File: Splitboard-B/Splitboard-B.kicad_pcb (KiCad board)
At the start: 2 copper layers, 185 x 150 mm, 83 parts, among them J1 USB_C_Receptacle, K1 KEYSW, K10 KEYSW, K11 KEYSW, K12 KEYSW, K13 KEYSW, K14 KEYSW, K15 KEYSW, K16 KEYSW, K17 KEYSW, K18 KEYSW, K19 KEYSW, K2 KEYSW, K20 KEYSW, K21 KEYSW, K22 KEYSW, K23 KEYSW, K24 KEYSW, K25 KEYSW, K26 KEYSW, K27 KEYSW, K28 KEYSW, K29 KEYSW, K3 KEYSW, K30 KEYSW, K31 KEYSW, K32 KEYSW, K33 KEYSW, K34 KEYSW, K35 KEYSW, K36 KEYSW, K37 KEYSW, K38 KEYSW, K4 KEYSW, K5 KEYSW, K6 KEYSW, K7 KEYSW, K8 KEYSW, K9 KEYSW, SW1 RotaryEncoder, U3 CR2013-MI2120

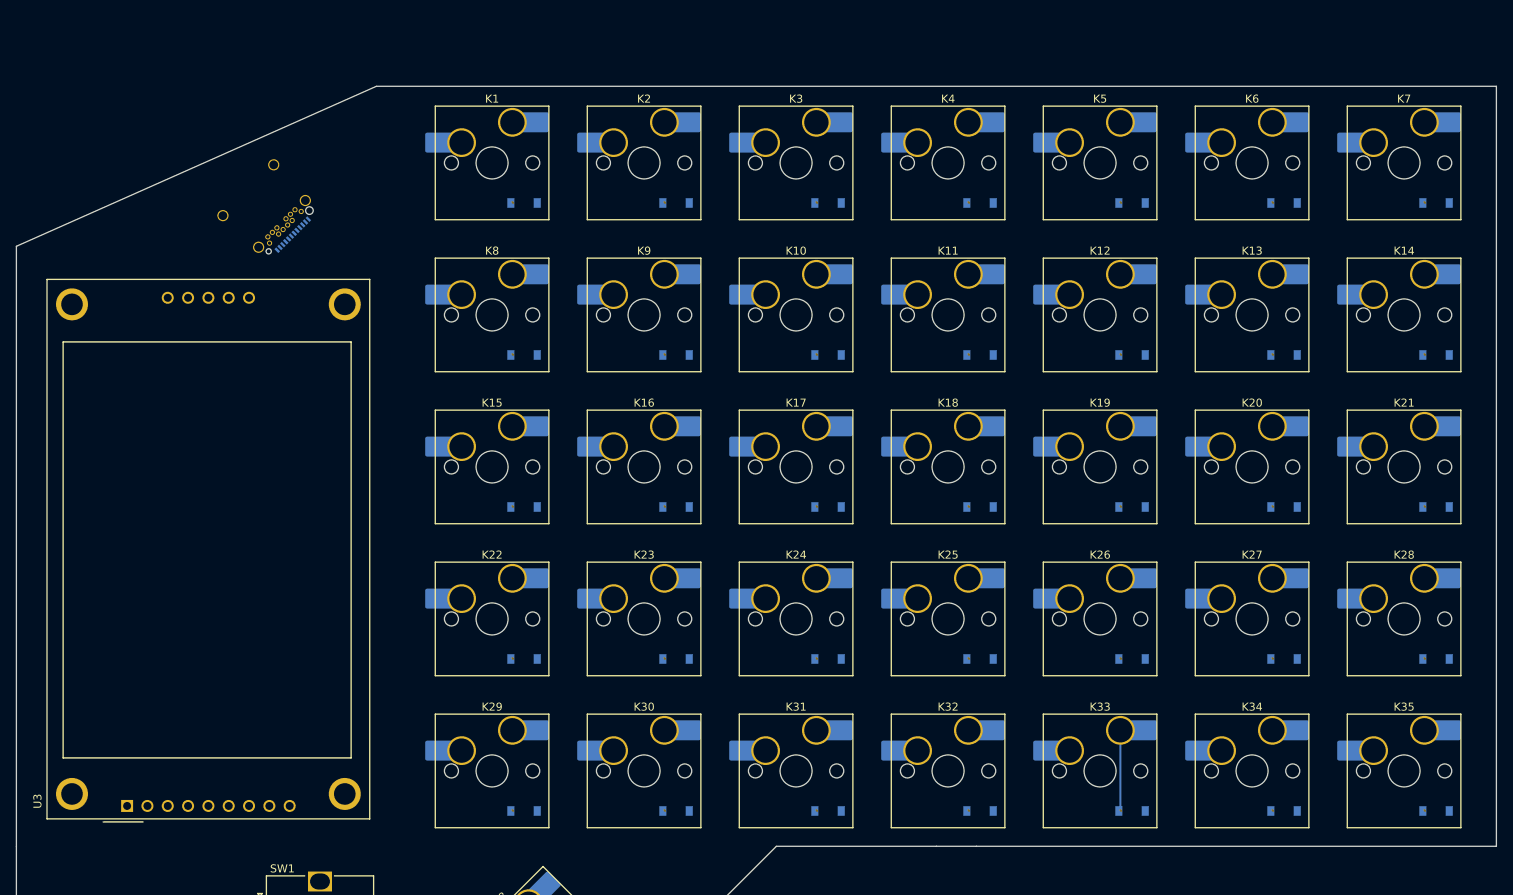
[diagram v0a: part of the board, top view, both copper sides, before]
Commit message: created 3d model for the keyboard as well as kbt1 acrylic models
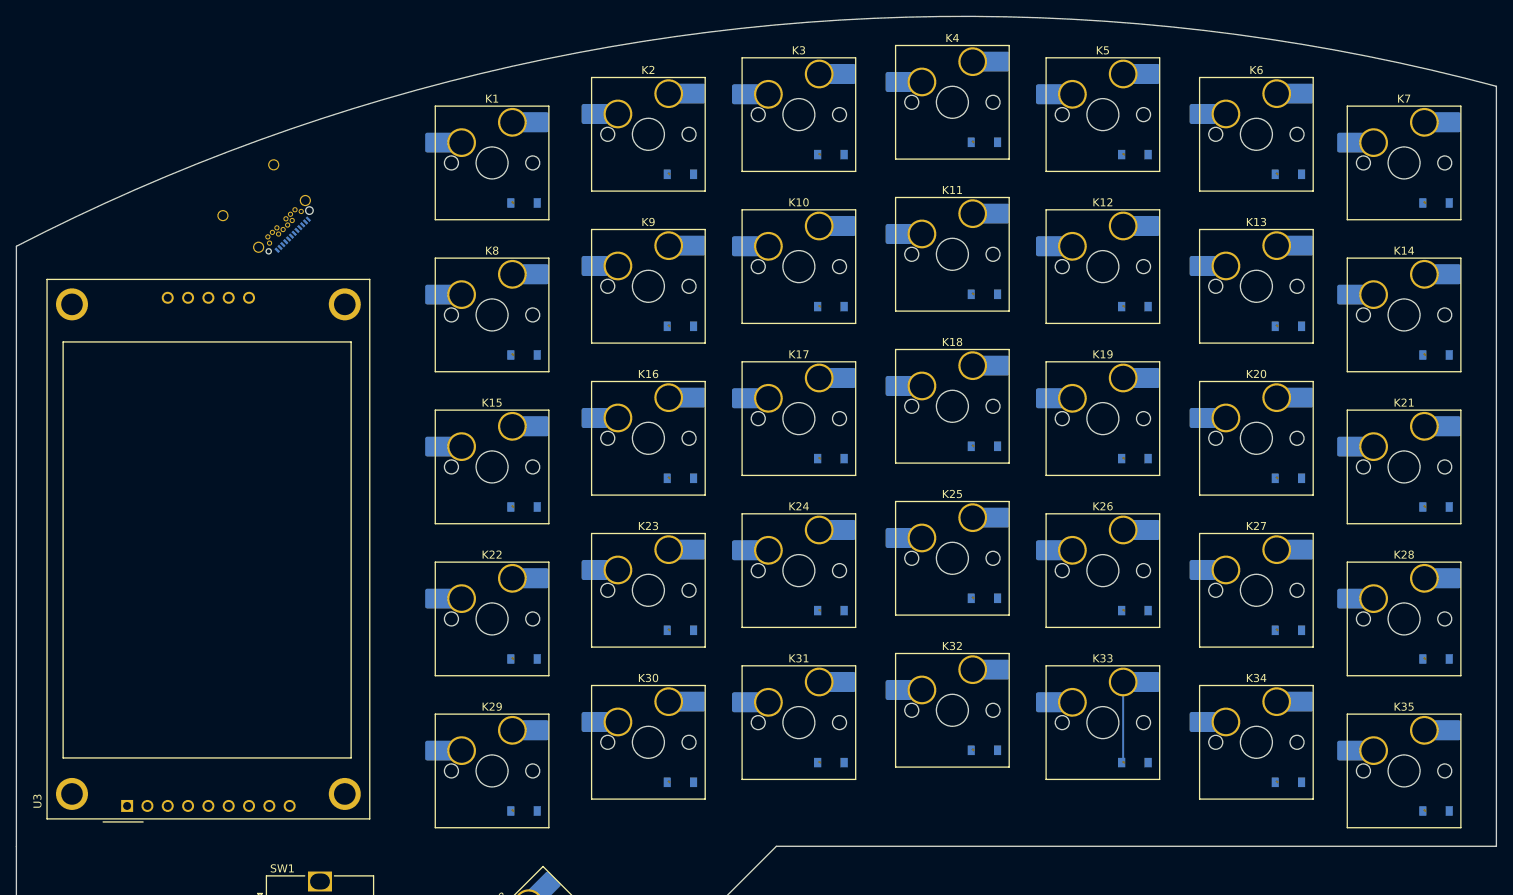
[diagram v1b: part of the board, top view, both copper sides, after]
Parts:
- moved D11 7.60 mm to (166.0, 61.0)
- moved D18 7.60 mm to (166.0, 80.0)
- moved D25 7.60 mm to (166.0, 99.0)
- moved D32 7.60 mm to (166.0, 118.0)
- moved D4 7.60 mm to (166.0, 42.0)
- moved K11 7.60 mm to (162.0, 56.0)
- moved K18 7.60 mm to (162.0, 75.0)
- moved K25 7.60 mm to (162.0, 94.0)
- moved K32 7.60 mm to (162.0, 113.0)
- moved K4 7.60 mm to (162.0, 37.0)
- moved D10 6.05 mm to (146.8, 62.5)
- moved D12 6.05 mm to (184.8, 62.5)
- moved D3 6.05 mm to (146.8, 43.5)
- moved D5 6.05 mm to (184.8, 43.5)
- moved K10 6.05 mm to (142.8, 57.5)
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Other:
- board size 185 x 150 mm -> 185 x 158.7 mm

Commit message: Keyboard changes (added split to other half, component footprints)
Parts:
- added U1: MCP23018-E/SP, 6:MCP23018-E&slash_SP, F.Cu at (65.0, 77.0)
- J1: footprint Connector_USB:USB_C_Receptacle_Amphenol_12401548E4-2A_CircularHoles -> Connector_USB:USB_C_Receptacle_GCT_USB4085
- moved H2 232.5 mm to (211.0, 34.0)
- moved H4 175.2 mm to (189.0, 126.0)
- moved H1 164.4 mm to (59.0, 53.0)
- moved H3 67.9 mm to (71.0, 160.0)
- moved J1 8.62 mm to (84.6, 50.8), turned to 20 degrees

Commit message: Added debugging header to splitboard B
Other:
- board text added: "ALL VIA INTERAL DIAMETERS NEED TO BE >= 5mm (for fly wiring) Also untented"
- board text added: "The switches unfortunately need to be re-spaced. They are 19mm apart from center to center, we need the horizontal distance to be 19mm, center to center distance will be greater than 19mm because of trig & stuff"
- board text added: "we need to consider creating more board for these holes consider the screw head that will rest on top of the hole"
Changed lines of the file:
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@@
   (gr_line (start 45 145) (end 45 130) (layer "Edge.Cuts") (width 0.1))
   (gr_arc (start 45 55) (mid 135.635806 27.756199) (end 230 35) (layer "Edge.Cuts") (width 0.1))
+  (gr_text "ALL VIA INTERAL DIAMETERS\nNEED TO BE >= 5mm (for fly wiring)\nAlso untented" (at 266.7 96.52) (layer "F.SilkS")
+    (effects (font (size 2 2) (thickness 0.3)))
+  )
+  (gr_text "The switches unfortunately need to be re-spaced.\nThey are 19mm apart from center to center, we need\nthe horizontal distance to be 19mm, center to center\ndistance will be greater than 19mm because of trig & stuff" (at 281.94 45.72) (layer "F.SilkS")
+    (effects (font (size 2 2) (thickness 0.3)))
+  )
+  (gr_text "we need to consider creating more board for these holes\nconsider the screw head that will rest on top of the hole" (at 210.82 139.7) (layer "F.SilkS")
+    (effects (font (size 1.5 1.5) (thickness 0.3)))
+  )
   (segment (start 145.35 100.43) (end 145.46 100.54) (width 0.25) (layer "F.Cu") (net 1))
   (segment (start 145.35 62.43) (end 145.46 62.54) (width 0.25) (layer "F.Cu") (net 1))

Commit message: Routing PCB
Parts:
- added C1: 100nF, Capacitor_SMD:C_0805_2012Metric, B.Cu at (93.8, 137.5)
- added C2: .01uF, Capacitor_SMD:C_0805_2012Metric, B.Cu at (63.5, 138.5)
- added C3: .01uF, Capacitor_SMD:C_0805_2012Metric, B.Cu at (66.8, 142.2)
- added C4: 100nF, Capacitor_SMD:C_0805_2012Metric, B.Cu at (75.5, 102.0)
- added C5: 100nF, Capacitor_SMD:C_0805_2012Metric, B.Cu at (88.2, 97.2)
- added C6: 10u, Capacitor_SMD:C_0805_2012Metric, B.Cu at (74.5, 58.2)
- added C7: 10u, Capacitor_SMD:C_0805_2012Metric, B.Cu at (72.5, 62.0)
- added D39: D_Schottky, Diode_SMD:D_SOD-123, B.Cu at (81.0, 62.0)
- added FB1: 100 @ 100 MHz, Resistor_SMD:R_0805_2012Metric, B.Cu at (76.2, 62.0)
- added J2: Conn_01x09, Connector_PinHeader_2.54mm:PinHeader_1x09_P2.54mm_Horizontal, F.Cu at (63.9, 93.9)
- added R1: 4K7, Resistor_SMD:R_0805_2012Metric, B.Cu at (89.0, 103.5)
- added R2: 4K7, Resistor_SMD:R_0805_2012Metric, B.Cu at (89.0, 106.0)
- added R3: 10k, Resistor_SMD:R_0805_2012Metric, B.Cu at (93.8, 142.8)
- added R4: 10k, Resistor_SMD:R_0805_2012Metric, B.Cu at (70.5, 133.5)
- added R5: 10k, Resistor_SMD:R_0805_2012Metric, B.Cu at (70.5, 137.5)
- added R6: 10k, Resistor_SMD:R_0805_2012Metric, B.Cu at (70.8, 146.2)
- added R7: 10k, Resistor_SMD:R_0805_2012Metric, B.Cu at (71.0, 142.5)
- added U2: MCP23017_SP, Package_DIP:DIP-28_W7.62mm, B.Cu at (85.8, 75.5)
- D36, D37, D38: moved to B.Cu
- J1: footprint Connector_USB:USB_C_Receptacle_GCT_USB4085 -> Connector_USB:USB_C_Receptacle_Amphenol_12401548E4-2A
- SW1: footprint Rotary_Encoder:RotaryEncoder_Alps_EC12E_Vertical_H20mm -> Rotary_Encoder:RotaryEncoder_Alps_EC11E-Switch_Vertical_H20mm
- U1: value MCP23018-E/SP -> CR2013-MI2120; footprint 6:MCP23018-E&slash_SP -> Display:CR2013-MI2120
- U3: value CR2013-MI2120 -> AMS1117-3.3; footprint Display:CR2013-MI2120 -> Package_TO_SOT_SMD:SOT-223-3_TabPin2; moved to B.Cu
- moved D38 71.1 mm to (117.3, 143.2), turned to -135 degrees
- moved U3 69.8 mm to (63.2, 55.2), turned to 0 degrees
- moved D37 56.0 mm to (103.9, 156.6), turned to -135 degrees
- moved U1 52.7 mm to (61.0, 129.5), turned to 90 degrees
- moved D36 39.6 mm to (90.5, 170.0), turned to -135 degrees
- moved H1 10.8 mm to (49.8, 58.5)
- moved J1 3.32 mm to (84.2, 47.5)
- moved H2 0.79 mm to (211.8, 33.8)
- moved D1 0.68 mm to (109.0, 50.0)
- moved D15 0.68 mm to (109.0, 88.0)
- moved D22 0.68 mm to (109.0, 107.0)
- moved D29 0.68 mm to (109.0, 126.0)
- moved D8 0.68 mm to (109.0, 69.0)
- moved K1 0.68 mm to (105.0, 45.0)
- moved K15 0.68 mm to (105.0, 83.0)
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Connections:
- J1 pad A1: Net-(J1-PadA1) -> GND
- J1 pad A12: Net-(J1-PadA1) -> GND
- J1 pad A4: Net-(J1-PadA4) -> VBUS
- J1 pad A5: unconnected-(J1-PadA5) -> /MOSI
- J1 pad A6: unconnected-(J1-PadA6) -> /SDA
- J1 pad A7: unconnected-(J1-PadA7) -> /SCL
- J1 pad A8: unconnected-(J1-PadA8) -> /SCK
- J1 pad A9: Net-(J1-PadA4) -> VBUS
- J1 pad B1: Net-(J1-PadA1) -> GND
- J1 pad B12: Net-(J1-PadA1) -> GND
- J1 pad B4: Net-(J1-PadA4) -> VBUS
- J1 pad B5: unconnected-(J1-PadB5) -> /MOSI
- J1 pad B6: unconnected-(J1-PadB6) -> /SDA
- J1 pad B7: unconnected-(J1-PadB7) -> /SCL
- J1 pad B8: unconnected-(J1-PadB8) -> /SCK
- J1 pad B9: Net-(J1-PadA4) -> VBUS
- J1 pad S1: unconnected-(J1-PadS1) -> GND
- SW1 pad A: unconnected-(SW1-PadA) -> Net-(R4-Pad2)
- SW1 pad B: unconnected-(SW1-PadB) -> Net-(R6-Pad2)
- SW1 pad C: unconnected-(SW1-PadC) -> GND
- U1 pad 1: unconnected-(U1-Pad1) -> VBUS
- U1 pad 2: unconnected-(U1-Pad2) -> GND
- U1 pad 3: unconnected-(U1-Pad3) -> /LCD2_CS
- U1 pad 4: unconnected-(U1-Pad4) -> /LCD2_RST
- U1 pad 5: unconnected-(U1-Pad5) -> /LCD2_DC
- U1 pad 6: unconnected-(U1-Pad6) -> /MOSI
- U1 pad 7: unconnected-(U1-Pad7) -> /SCK
- U1 pad 8: unconnected-(U1-Pad8) -> +3.3V
- U3 pad 1: unconnected-(U3-Pad1) -> GND
- U3 pad 2: unconnected-(U3-Pad2) -> +3.3V
- U3 pad 3: unconnected-(U3-Pad3) -> Net-(C6-Pad1)
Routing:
- net /row6: track 0.00 -> 417.0 mm
- net /row5: track 0.00 -> 249.8 mm, vias 0 -> 5
- net /col1: track 0.00 -> 247.3 mm
- net /row2: track 0.00 -> 237.1 mm, vias 0 -> 5
- net /row1: track 0.00 -> 235.3 mm, vias 0 -> 5
- net /row4: track 0.00 -> 232.4 mm, vias 0 -> 5
- net /col2: track 0.00 -> 232.4 mm
- net /row0: track 0.00 -> 218.9 mm, vias 0 -> 5
- net /col3: track 0.00 -> 218.5 mm
- net /row3: track 0.00 -> 214.3 mm, vias 0 -> 5
- net /col0: track 0.00 -> 210.0 mm
- net /col4: track 0.00 -> 209.9 mm
- net VBUS: track 0.00 -> 119.6 mm
- net /col5: track 0.00 -> 113.4 mm
- net /ENC_B: track 0.00 -> 82.2 mm, vias 0 -> 1
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- added copper zone on B.Cu, net +3.3V
- added copper zone on B.Cu, net GND

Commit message: Layout changes
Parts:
- moved H4 18.1 mm to (207.0, 128.0)
- moved H1 1.95 mm to (51.0, 57.0)
- moved H2 0.35 mm to (211.5, 33.5)
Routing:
- net +3.3V: track 61.1 -> 246.8 mm, vias 0 -> 4
- net GND: track 75.2 -> 237.0 mm, vias 1 -> 2
- net /SCL: track 0.00 -> 120.7 mm
- net /LCD2_RST: track 0.00 -> 120.6 mm, vias 0 -> 3
- net /SCK: track 0.00 -> 118.7 mm, vias 0 -> 1
- net /MOSI: track 0.00 -> 115.9 mm, vias 0 -> 1
- net /SDA: track 0.00 -> 115.1 mm, vias 0 -> 2
- net /LCD2_DC: track 0.00 -> 106.2 mm
- net /LCD2_CS: track 49.0 -> 107.9 mm
- net VBUS: track 119.6 -> 111.1 mm, vias 0 -> 1
- net /ENC_B: track 82.2 -> 89.7 mm
- net /ENC_A: track 81.5 -> 88.3 mm
- net /row0: track 218.9 -> 223.7 mm, vias 5 -> 6
- net /row1: track 235.3 -> 237.6 mm
- net /row2: track 237.1 -> 239.2 mm
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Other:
- board size 185 x 158.7 mm -> 185 x 161.7 mm
